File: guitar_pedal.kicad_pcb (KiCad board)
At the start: 2 copper layers, 89.5 x 81.3 mm, 114 parts, among them J1 Conn_01x02_Pin, J2 Conn_01x02_Pin, J3 Conn_01x02_Pin, Q1 2N3904, Q2 2N3904, Q3 2N3904, Q4 2N3904, Q5 2N3904, U1 LM358, U2 LM358, U3 LM358, U4 LM358, U5 LM358

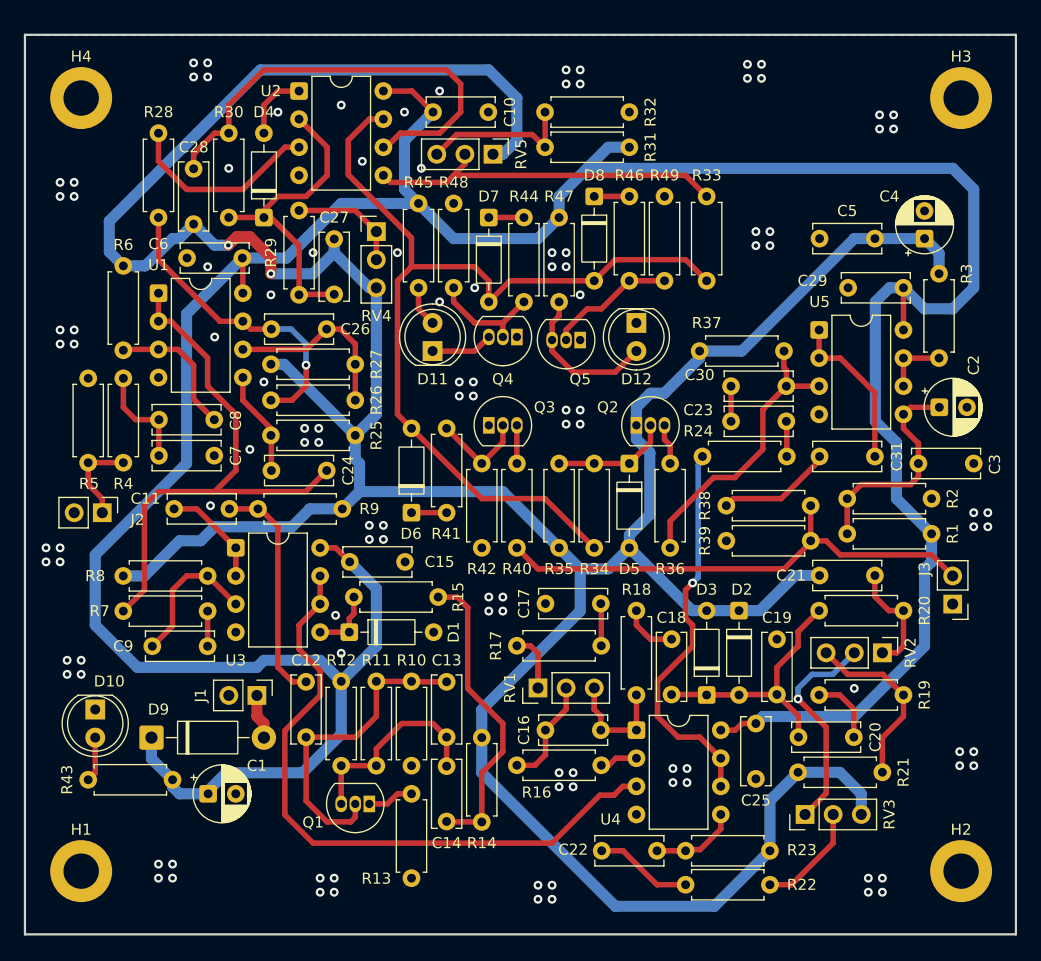
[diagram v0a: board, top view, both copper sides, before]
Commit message: replaced ceramic capacitors with polyester. Added stitching vias between top and bottom ground planes
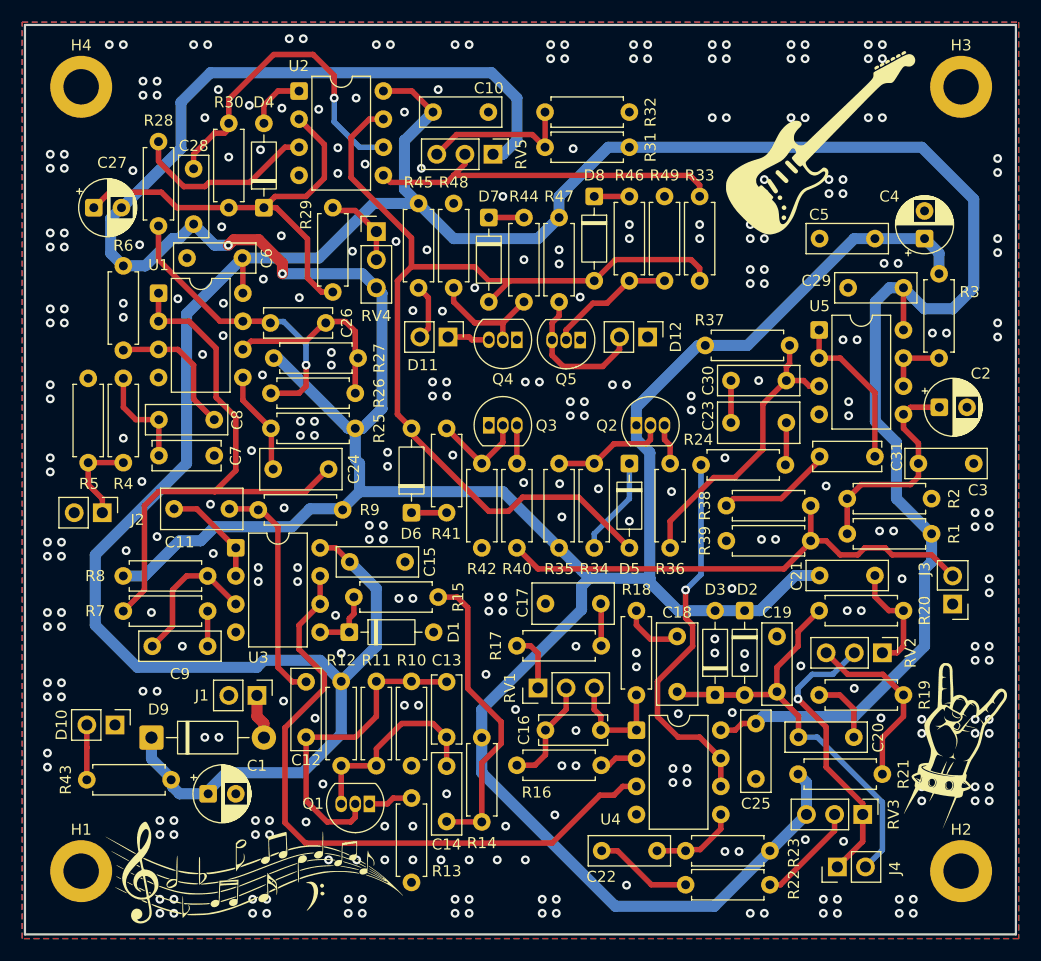
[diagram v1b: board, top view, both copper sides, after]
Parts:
- added G***: LOGO, LOGO, F.Cu at (102.7, 143.4)
- added G***: LOGO, LOGO, F.Cu at (166.1, 132.0)
- added G***: LOGO, LOGO, F.Cu at (154.1, 77.5)
- added J4: Conn_01x02_Pin, Connector_PinHeader_2.54mm:PinHeader_1x02_P2.54mm_Vertical, F.Cu at (155.4, 142.9)
- C10, C12, C14, C15, C19, C20, C21, C22, C25, C28, C29, C3, C30, C5, C6, C8, C9: footprint Capacitor_THT:C_Disc_D6.0mm_W2.5mm_P5.00mm -> Capacitor_THT:C_Rect_L7.2mm_W2.5mm_P5.00mm_FKS2_FKP2_MKS2_MKP2
- C11, C17, C18, C23, C24: footprint Capacitor_THT:C_Disc_D6.0mm_W2.5mm_P5.00mm -> Capacitor_THT:C_Rect_L7.2mm_W3.5mm_P5.00mm_FKS2_FKP2_MKS2_MKP2
- C27: footprint Capacitor_THT:C_Disc_D6.0mm_W2.5mm_P5.00mm -> Capacitor_THT:CP_Radial_D5.0mm_P2.50mm
- D10, D11, D12: footprint LED_THT:LED_D5.0mm -> Connector_PinHeader_2.54mm:PinHeader_1x02_P2.54mm_Vertical
- R34: value 4.7k -> 47k
- R35: value 47k -> 470k
- R38: value 1k -> 10k
- moved C27 21.9 mm to (88.3, 83.3), turned to 0 degrees
- moved RV3 5.21 mm to (157.7, 138.1), turned to -90 degrees
- moved R29 3.06 mm to (109.9, 90.9)
- moved D10 2.27 mm to (90.2, 130.0)
- moved D11 1.89 mm to (120.3, 95.0), turned to -90 degrees
- moved D12 1.63 mm to (138.3, 95.0)
- moved H3 1.02 mm to (166.6, 72.4)
- moved H4 1.02 mm to (87.1, 72.4)
- moved D4 0.89 mm to (103.6, 83.3)
- moved R30 0.89 mm to (100.5, 83.3)
- moved R24 0.77 mm to (143.1, 106.6)
- moved D3 0.76 mm to (144.4, 127.3)
- moved R28 0.76 mm to (94.1, 85.0)
- moved R37 0.72 mm to (151.1, 95.8)
- moved R26 0.64 mm to (104.3, 100.1)
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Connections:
- C27 pad 1: +4.5V -> Net-(D4-K)
- C27 pad 2: Net-(D4-K) -> +4.5V
- D5 pad 2: +4.5V -> Net-(D5-A)
- D6 pad 2: Net-(D6-A) -> Net-(D5-A)
- D7 pad 2: Net-(D6-A) -> Net-(D5-A)
- D8 pad 2: Net-(D6-A) -> Net-(D5-A)
- Q2 pad 2: Net-(D5-K) -> Net-(Q2-B)
- R33 pad 2: Net-(D6-A) -> Net-(D5-A)
- R34 pad 1: Net-(D6-A) -> Net-(D5-K)
- R34 pad 2: Net-(D5-K) -> Net-(Q2-B)
- R35 pad 2: Net-(D5-K) -> Net-(Q2-B)
- U2 pad 7: Net-(D6-A) -> Net-(D5-A)
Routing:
- net Net-(D5-A): track 0.00 -> 90.2 mm
- net Net-(D6-A): track 85.9 -> 0.00 mm
- net Net-(D2-A): track 23.4 -> 40.5 mm
- net Net-(D4-K): track 28.2 -> 41.5 mm
- net Net-(U2B--): track 41.5 -> 29.9 mm, vias 0 -> 1
- net Net-(Q2-B): track 0.00 -> 10.4 mm
- net +4.5V: track 310.9 -> 302.4 mm
- net Net-(J4-Pin_1): track 19.7 -> 25.9 mm
- net +9V: track 283.4 -> 279.8 mm
- net Net-(R29-Pad2): track 10.3 -> 7.37 mm
- net Net-(D11-A): track 3.70 -> 5.64 mm
- net Net-(D11-K): track 5.61 -> 3.79 mm
- net Net-(D5-K): track 10.6 -> 8.94 mm
- net Net-(U1A--): track 50.4 -> 51.6 mm
- net Net-(D10-A): track 4.07 -> 5.13 mm
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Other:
- board size 89.5 x 81.3 mm -> 89.5 x 82.2 mm

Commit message: drop files from .gitignore
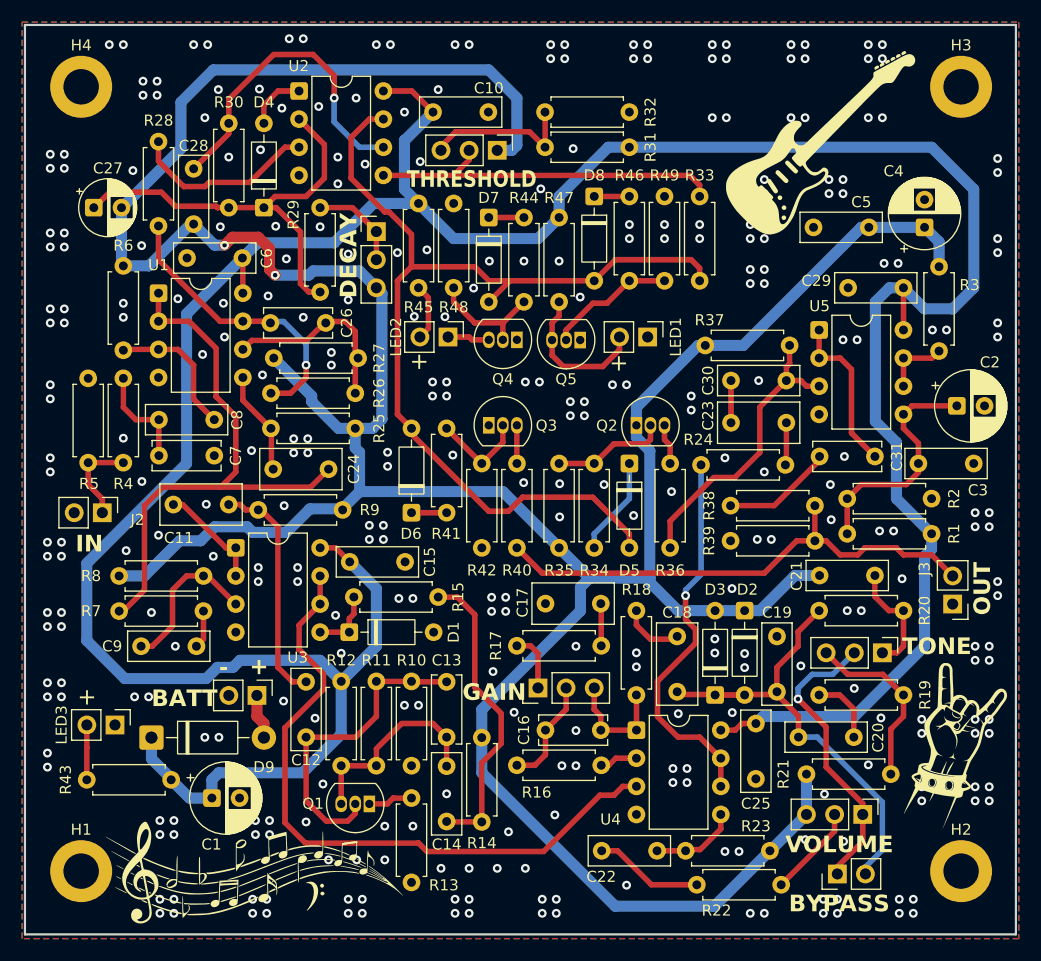
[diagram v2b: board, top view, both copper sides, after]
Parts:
- C1, C2, C4: footprint Capacitor_THT:CP_Radial_D5.0mm_P2.50mm -> Capacitor_THT:CP_Radial_D6.3mm_P2.50mm
- moved C2 1.59 mm to (166.2, 101.2)
- moved C5 1.15 mm to (153.3, 85.1)
- moved R29 1.14 mm to (108.7, 90.9)
- moved C4 1.02 mm to (163.3, 85.1)
- moved R22 1.02 mm to (150.4, 144.5)
- moved C9 1.01 mm to (97.5, 122.9)
- moved R21 0.76 mm to (160.3, 134.5)
- moved J4 0.63 mm to (155.4, 143.5)
- moved R3 0.63 mm to (164.6, 96.3)
- moved RV5 0.52 mm to (124.7, 78.1)
- moved C1 0.51 mm to (98.9, 136.7)
- moved C11 0.40 mm to (95.5, 110.1)
- moved R38 0.38 mm to (145.8, 110.2)
- moved R39 0.38 mm to (145.8, 113.4)
- moved R7 0.38 mm to (90.6, 119.8)
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- renumbered D12 to LED1, D11 to LED2, D10 to LED3
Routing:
- net +9V: track 279.8 -> 283.9 mm
- net +4.5V: track 302.4 -> 304.8 mm
- net Net-(U5B-+): track 20.1 -> 21.5 mm
- net Net-(C22-Pad1): track 8.85 -> 9.87 mm
- net Net-(D4-K): track 41.5 -> 40.5 mm
- net Net-(U3A-+): track 13.1 -> 14.1 mm
- net Net-(R22-Pad1): track 9.33 -> 8.35 mm
- net Net-(D5-A): track 90.2 -> 91.2 mm
- net Net-(R29-Pad2): track 7.37 -> 8.01 mm
- net Net-(J4-Pin_1): track 25.9 -> 26.6 mm
- net Net-(D2-A): track 40.5 -> 41.1 mm
- net Net-(U3B--): track 60.1 -> 60.7 mm
- net Net-(U2B--): track 29.9 -> 29.4 mm
- net Net-(C9-Pad1): track 3.18 -> 3.69 mm
- net GND: vias 318 -> 325
